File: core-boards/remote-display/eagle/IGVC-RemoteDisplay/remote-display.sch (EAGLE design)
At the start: 20 parts, among them IC1 ATMEGA2560-15AU, J1 ULCD-144G2, SW1 SPST_TACT-EVQQ2, U1 CC1101-MODULE, X1 16MHz, X2 MSTBA2

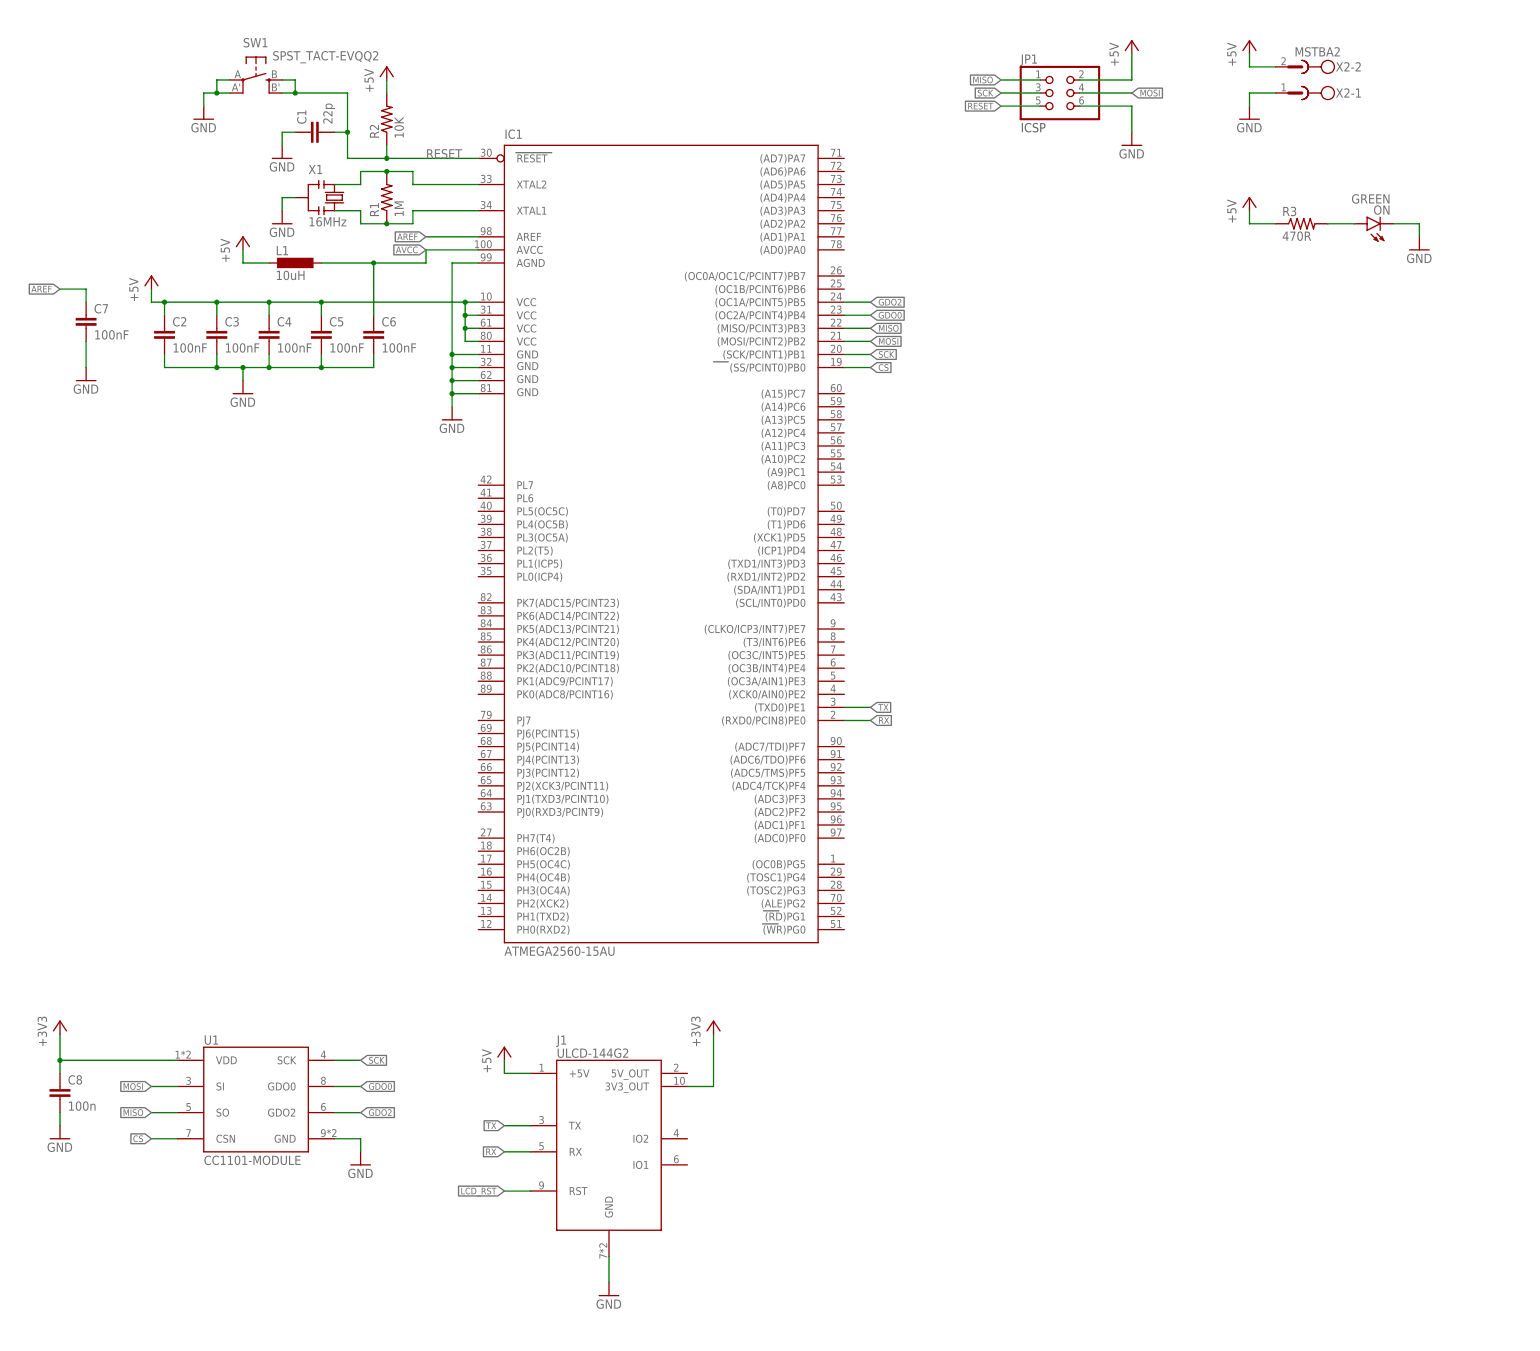
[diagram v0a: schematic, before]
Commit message: Replaced the MEGA2560 with a MEGA328p
This is just an option; if there are reasons for using the 2560, this can certainly be reverted
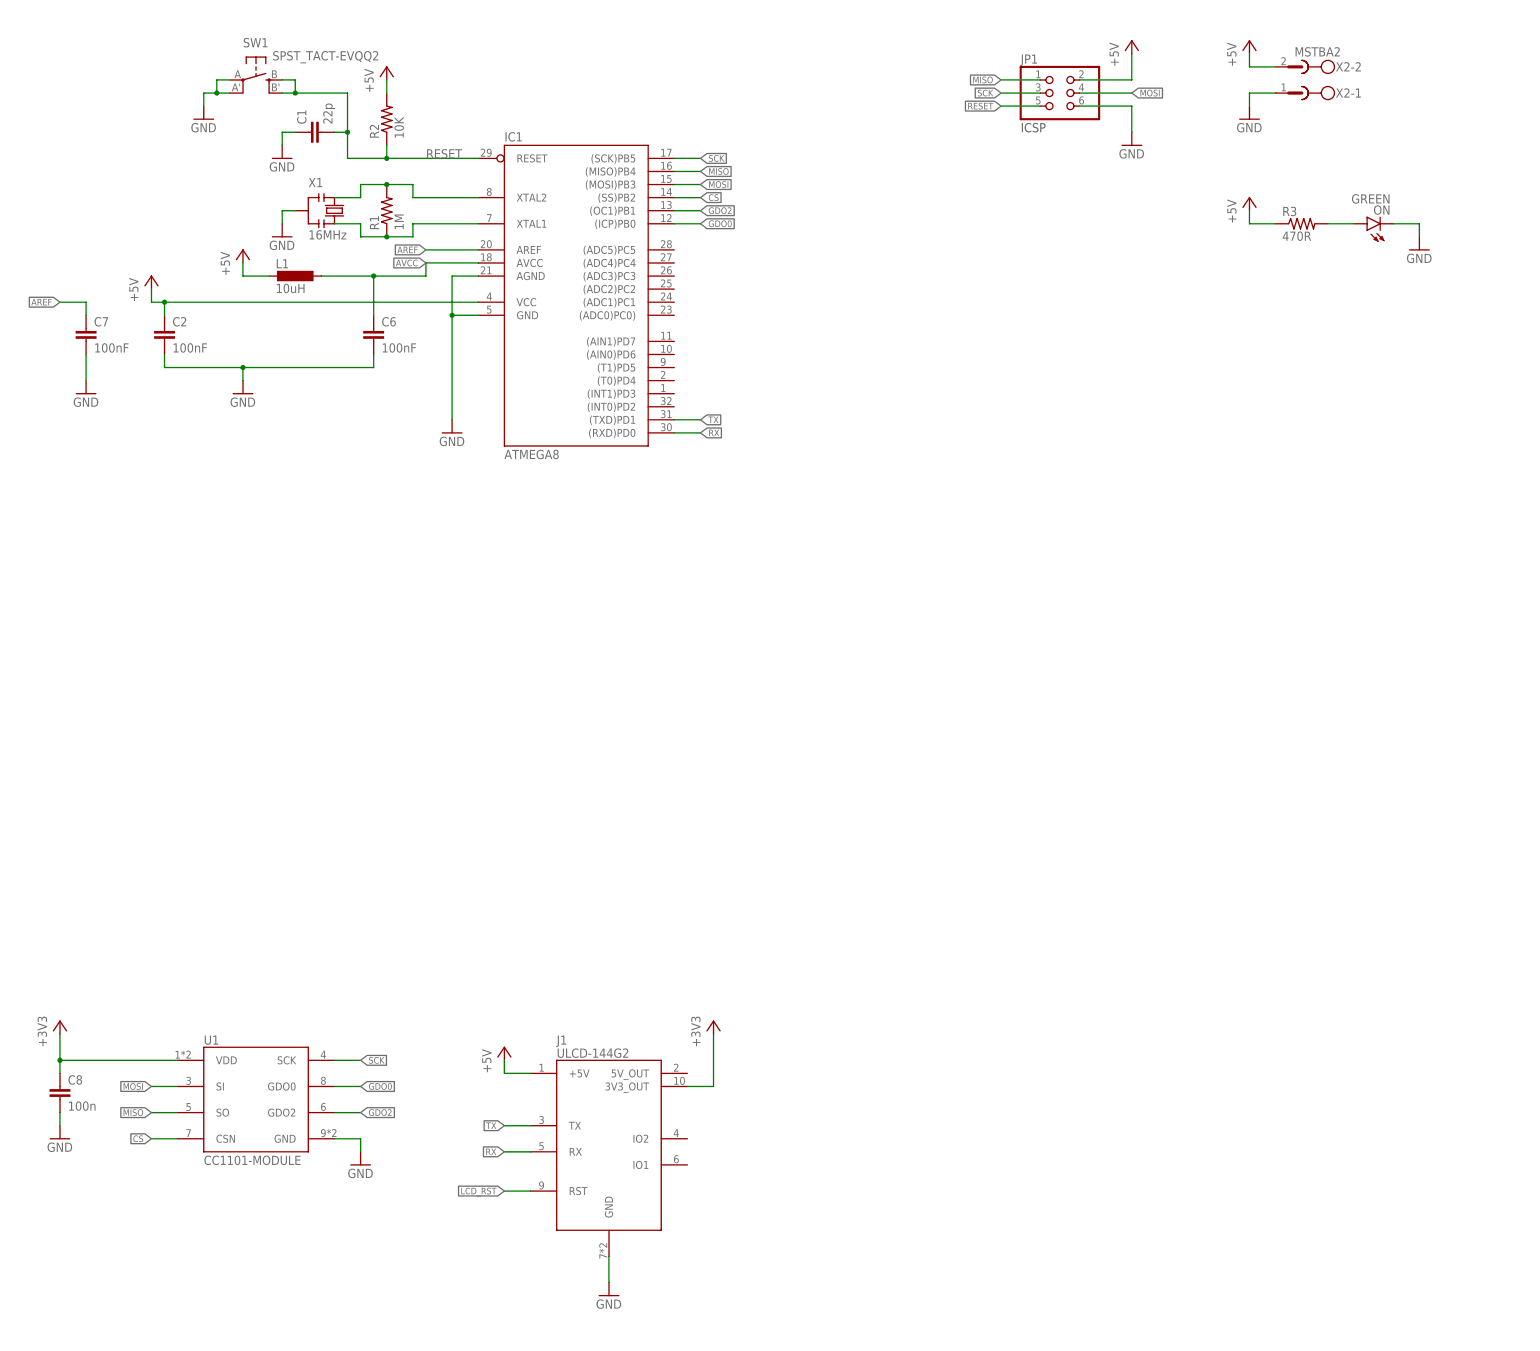
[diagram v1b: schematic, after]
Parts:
- removed C3, C4, C5: 100nF, resistor:C-EUC0603
- IC1: value ATMEGA2560-15AU -> ATMEGA8; device IGVC-Remote:ATMEGA2560-16AU -> atmel:AT90S4433A
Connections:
- net +5V: no longer C3.1, C4.1, C5.1, IC1.VCC1, IC1.VCC2, IC1.VCC3
- net CS: now also IC1.(SS)PB2; no longer IC1.(SS/PCINT0)PB0
- net GDO0: now also IC1.(ICP)PB0; no longer IC1.(OC2A/PCINT4)PB4
- net GDO2: now also IC1.(OC1)PB1; no longer IC1.(OC1A/PCINT5)PB5
- net GND: no longer C3.2, C4.2, C5.2, IC1.GND1, IC1.GND2, IC1.GND3
- net MISO: now also IC1.(MISO)PB4; no longer IC1.(MISO/PCINT3)PB3
- net MOSI: now also IC1.(MOSI)PB3; no longer IC1.(MOSI/PCINT2)PB2
- net RX: now also IC1.(RXD)PD0; no longer IC1.(RXD0/PCIN8)PE0
- net SCK: now also IC1.(SCK)PB5; no longer IC1.(SCK/PCINT1)PB1
- net TX: now also IC1.(TXD)PD1; no longer IC1.(TXD0)PE1
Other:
- moved on the sheet: C7, L1, R1, X1

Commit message: 20191117 Reworked schematic
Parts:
- removed J1: ULCD-144G2, IGVC-Remote:ULCD-144G2
- removed X2: MSTBA2, con-phoenix-508:MSTBA2
- added C10, C11: 10uF, rcl:C-EUC0603
- added C3: 0.1uF, resistor:C-EUC0603
- added C4: 100uF, rcl:CPOL-USD
- added C5, C9: 1uF, rcl:C-EUC0603
- added J4: B2PS-VH(LF)(SN), RoboJackets-Connectors:B2PS-VH(LF)(SN)
- added R4: 47R, resistor:R-US_R0805
- added T1: R-78E5.0-1.0, MotorBoardDev:R-78E5.0-1.0
- added U2: ST7920, IGVC-Remote:ST7920
- added X3: (no value), IGVC-Connector:NRF24L01+PA+LNA
- C1: value 22p -> 22pF
- C2, C6, C7: value 100nF -> 0.1uF
- C8: value 100n -> 0.1uF
- U1: value CC1101-MODULE -> MIC550X; device IGVC-Remote:CC1101-MODULE -> IGVC-Regulator:MIC550X
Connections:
- removed net CS: IC1.(SS)PB2, U1.CSN
- removed net LCD_RST: J1.RST
- new net LCD_CS: U2.4
- new net N$3: R4.1, U2.19
- new net RF_CS: IC1.(SS)PB2, X3.CSN
- new net VCC: C10.1, C4.+, J4.2, T1.VIN
- net +3V3: now also C5.1, U1.OUT, X3.VCC; no longer J1.3V3_OUT, U1.VDD
- net +5V: now also C11.1, C3.1, C9.1, R4.2, T1.VOUT, U1.IN, U2.17, U2.2; no longer J1.+5V, X2-2.1
- net GDO0: now also X3.CE; no longer U1.GDO0
- net GDO2: now also X3.IRQ; no longer U1.GDO2
- net GND: now also C10.2, C11.2, C3.2, C4.-, C5.2, C9.2, J4.1, T1.GND, U2.1, U2.15, U2.20, X3.GND; no longer J1.GND, X2-1.1
- net MISO: now also X3.MISO; no longer U1.SO
- net MOSI: now also U2.5, X3.MOSI; no longer U1.SI
- net RX: no longer J1.RX
- net SCK: now also U2.6, X3.SCK; no longer U1.SCK
- net TX: no longer J1.TX
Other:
- note added: "Note: EN has an internal pull-down and can be left floating"
- moved on the sheet: C8, ON, R3

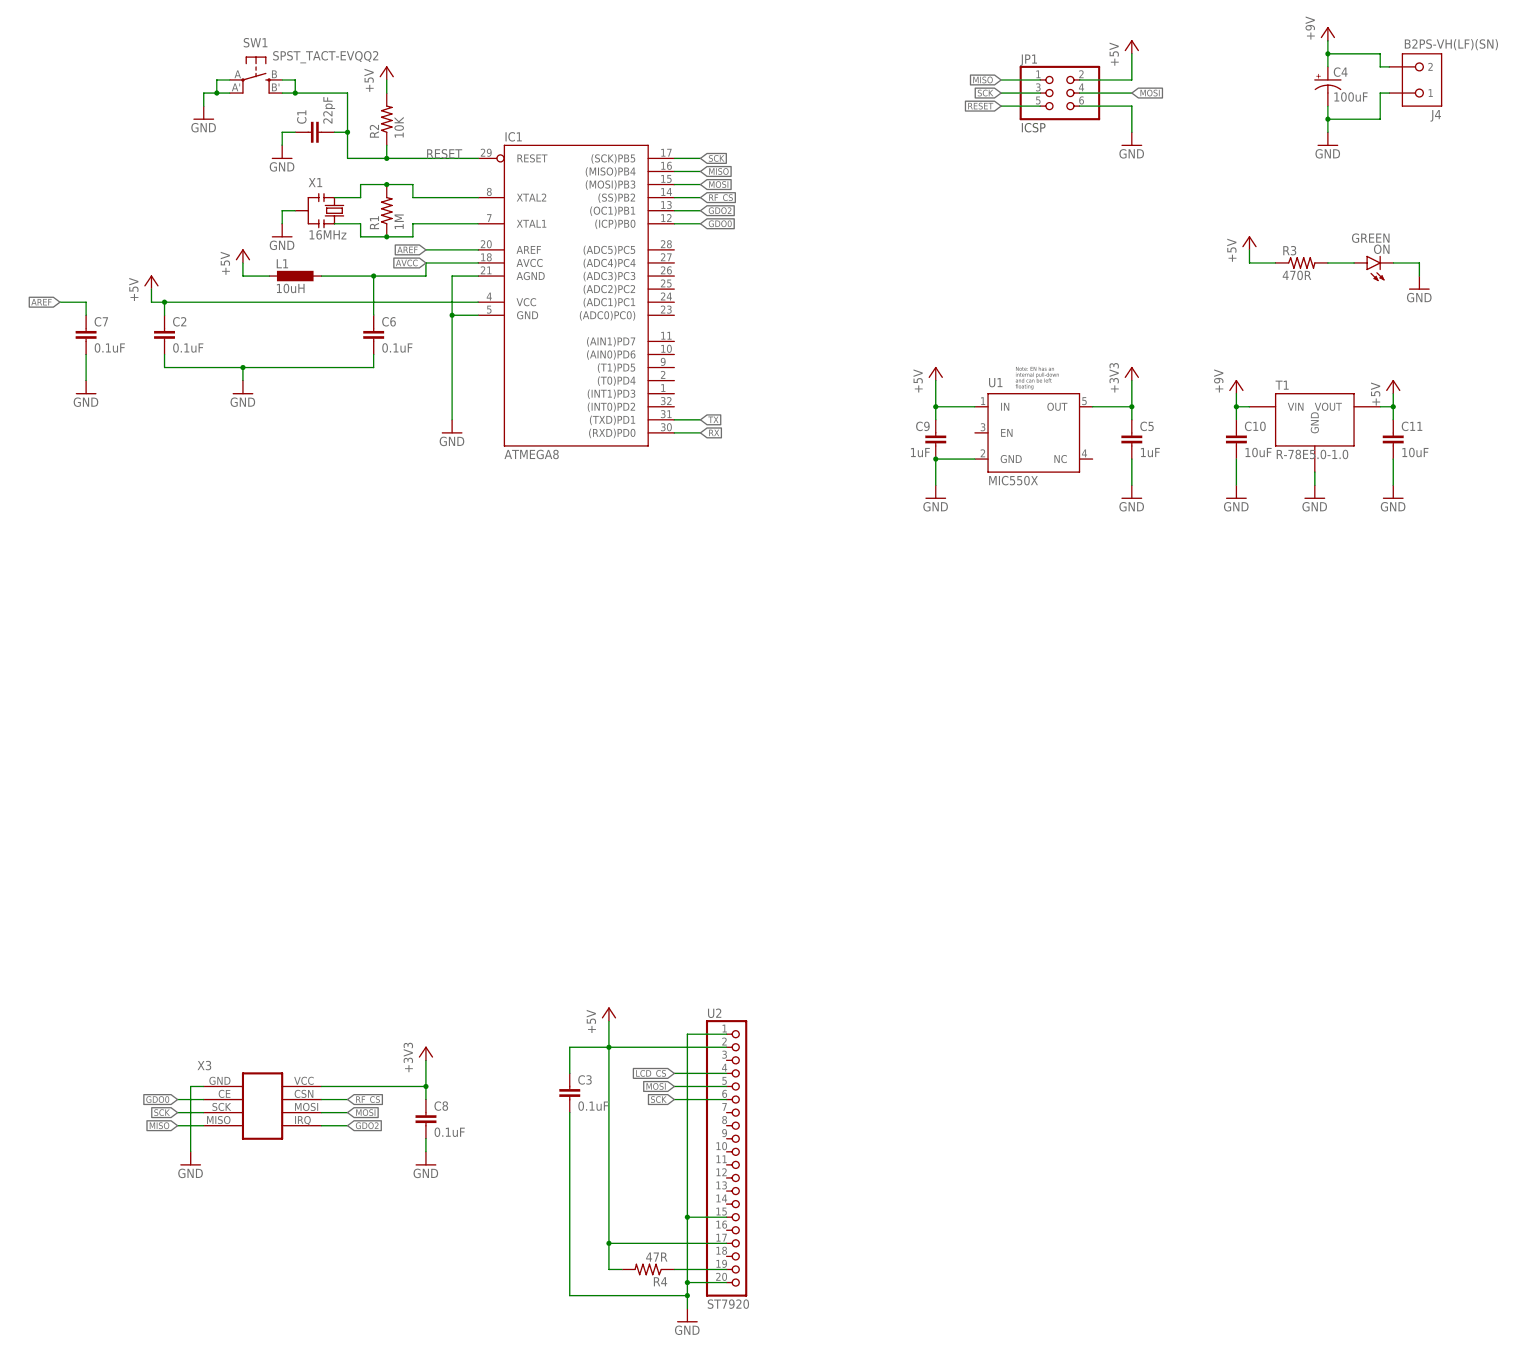
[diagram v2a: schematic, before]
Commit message: Finished routing, design review pending
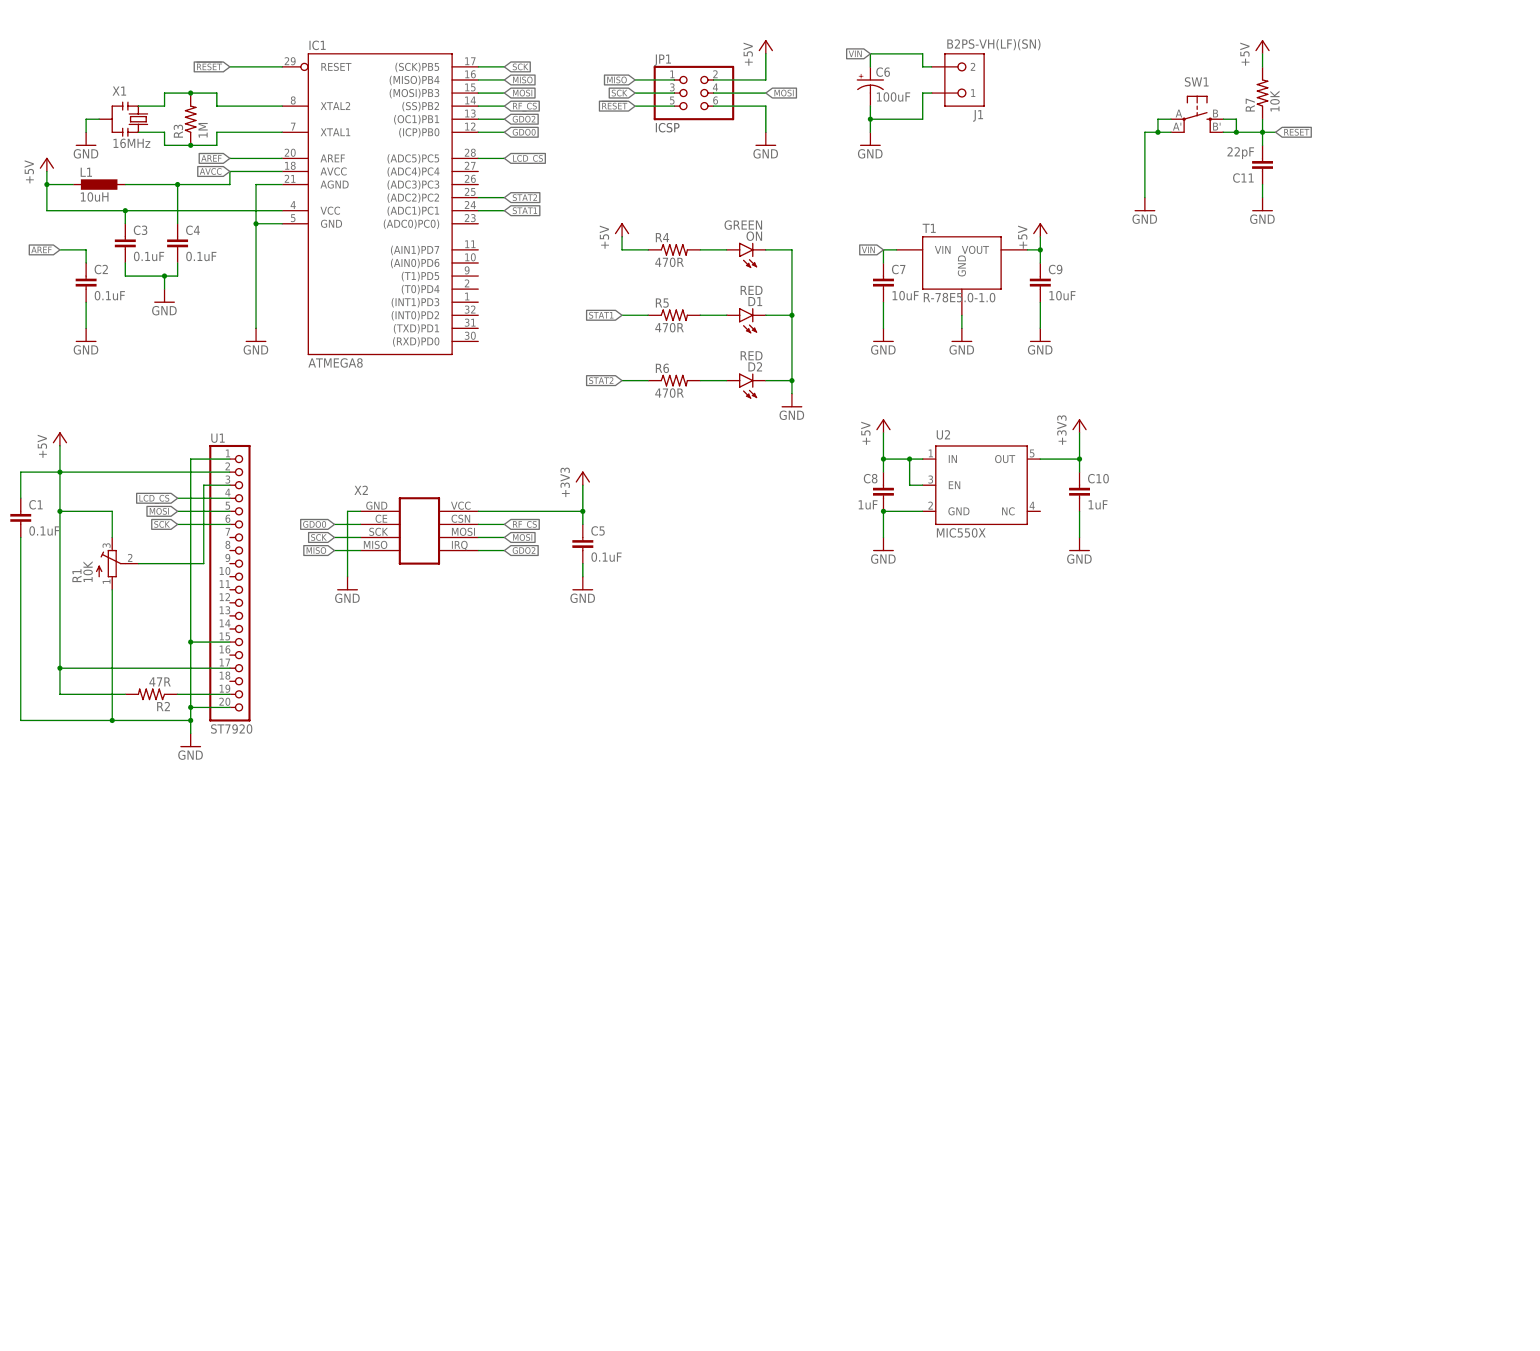
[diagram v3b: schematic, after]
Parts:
- removed J4: B2PS-VH(LF)(SN), RoboJackets-Connectors:B2PS-VH(LF)(SN)
- removed X3: (no value), IGVC-Connector:NRF24L01+PA+LNA
- added D1, D2: RED, led:LEDCHIP-LED0805
- added J1: B2PS-VH(LF)(SN), RoboJackets-Connectors:B2PS-VH(LF)(SN)
- added R5, R6: 470R, resistor:R-US_R0603
- added R7: 10K, resistor:R-US_R0603
- added U$1: ROBOBUZZ1.0X, RoboJackets-Aesthetics:ROBOBUZZ1.0X
- added X2: (no value), IGVC-Connector:NRF24L01+PA+LNA
- C1: value 22pF -> 0.1uF
- C10: value 10uF -> 1uF
- C11: value 10uF -> 22pF; device rcl:C-EUC0603 -> resistor:C-EUC0603
- C4: value 100uF -> 0.1uF; device rcl:CPOL-USD -> resistor:C-EUC0603
- C5: value 1uF -> 0.1uF; device rcl:C-EUC0603 -> resistor:C-EUC0603
- C6: value 0.1uF -> 100uF; device resistor:C-EUC0603 -> rcl:CPOL-USD
- C7: value 0.1uF -> 10uF; device resistor:C-EUC0603 -> rcl:C-EUC0603
- C8: value 0.1uF -> 1uF; device resistor:C-EUC0603 -> rcl:C-EUC0603
- C9: value 1uF -> 10uF
- R1: value 1M -> 10K; device resistor:R-US_R0603 -> adafruit:TRIMPOT3386
- R2: value 10K -> 47R; device resistor:R-US_R0603 -> resistor:R-US_R0805
- R3: value 470R -> 1M
- R4: value 47R -> 470R; device resistor:R-US_R0805 -> resistor:R-US_R0603
- U1: value MIC550X -> ST7920; device IGVC-Regulator:MIC550X -> IGVC-Remote:ST7920
- U2: value ST7920 -> MIC550X; device IGVC-Remote:ST7920 -> IGVC-Regulator:MIC550X
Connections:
- removed net RESET: C1.2, IC1.RESET, JP1.5, R2.1, SW1.S, SW1.S1
- removed net RX: IC1.(RXD)PD0
- removed net TX: IC1.(TXD)PD1
- removed net VCC: C10.1, C4.+, J4.2, T1.VIN
- new net !RESET: C11.2, IC1.RESET, JP1.5, R7.1, SW1.S, SW1.S1
- new net CONTRAST: R1.S, U1.3
- new net STAT1: IC1.(ADC1)PC1, R5.1
- new net STAT1_LED: D1.A, R5.2
- new net STAT2: IC1.(ADC2)PC2, R6.1
- new net STAT2_LED: D2.A, R6.2
- new net VIN: C6.+, C7.1, J1.2, T1.VIN
- net +3V3: now also C10.1, U2.OUT, X2.VCC; no longer C8.1, U1.OUT, X3.VCC
- net +5V: now also C1.1, C8.1, R1.E, R4.1, R7.2, U1.17, U1.2, U2.EN, U2.IN; no longer C11.1, C2.1, R3.1, R4.2, U1.IN, U2.17, U2.2
- net AREF: now also C2.1; no longer C7.1
- net AVCC: now also C4.1; no longer C6.1
- net GDO0: now also X2.CE; no longer X3.CE
- net GDO2: now also X2.IRQ; no longer X3.IRQ
- net GND: now also C1.2, C11.1, C4.2, C6.-, D1.C, D2.C, J1.1, R1.A, U1.1, U1.15, U1.20, U2.GND, X2.GND; no longer C1.1, C11.2, C4.-, C6.2, J4.1, U1.GND, U2.1, U2.15, U2.20, X3.GND
- net LCD_CS: now also IC1.(ADC5)PC5, U1.4; no longer U2.4
- net MISO: now also X2.MISO; no longer X3.MISO
- net MOSI: now also U1.5, X2.MOSI; no longer U2.5, X3.MOSI
- net N$3: now also R2.1, U1.19; no longer R4.1, U2.19
- net PWR_LED: now also R4.2; no longer R3.2
- net RF_CS: now also X2.CSN; no longer X3.CSN
- net SCK: now also U1.6, X2.SCK; no longer U2.6, X3.SCK
- net XTAL1: now also R3.1; no longer R1.1
- net XTAL2: now also R3.2; no longer R1.2
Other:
- note removed: "Note: EN has an internal pull-down and can be left floating"
- moved on the sheet: C1, C10, C11, C2, C3, C5, C7, C8, C9, IC1, JP1, L1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
